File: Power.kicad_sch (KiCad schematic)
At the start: 56 parts, among them IC701 TPS63021DSJR, U702 TLV9304IDR

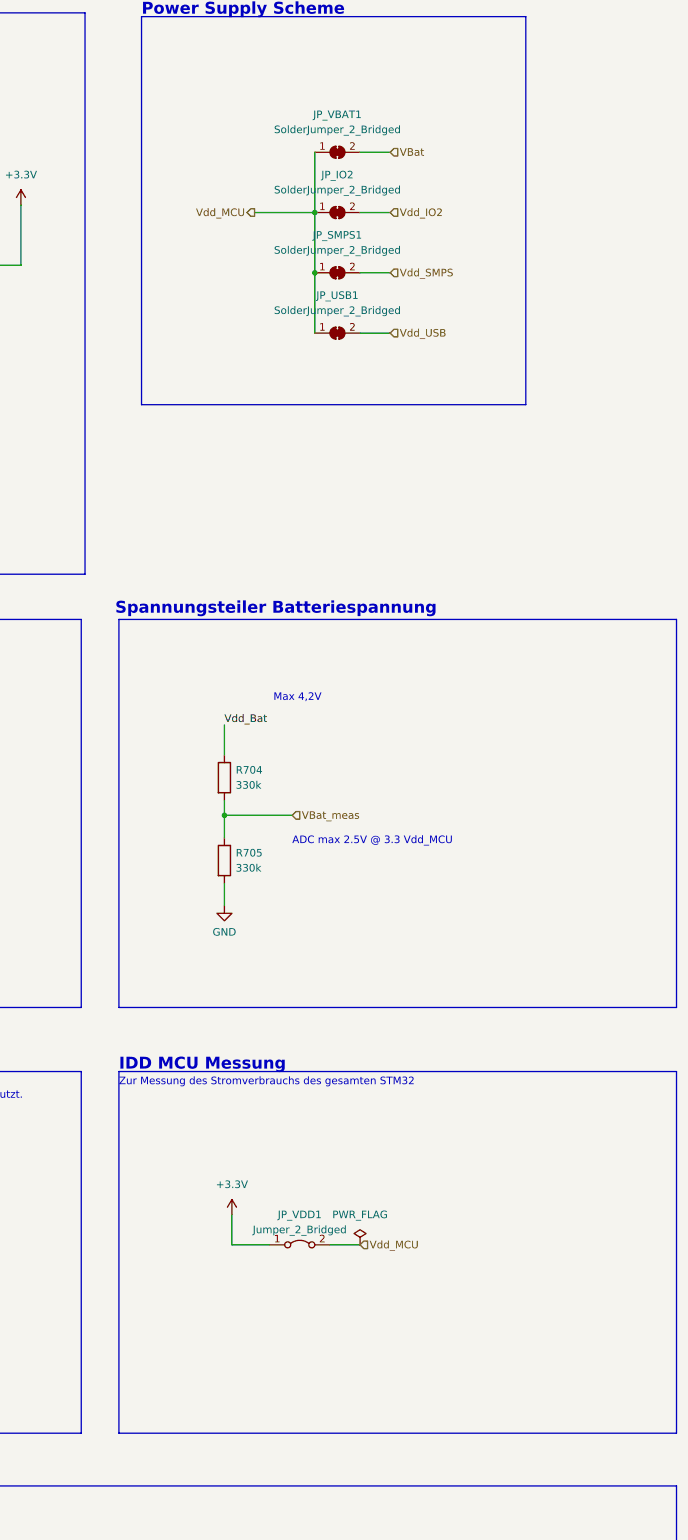
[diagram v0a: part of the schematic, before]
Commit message: Add FC0V104ZFTBR24 component library files
Added symbol, footprint, 3D model, and documentation files for the Supercap (FC0V104ZFTBR24) component across multiple EDA tool formats. Also updated schematic files and project backups, and removed obsolete autosave and backup files.
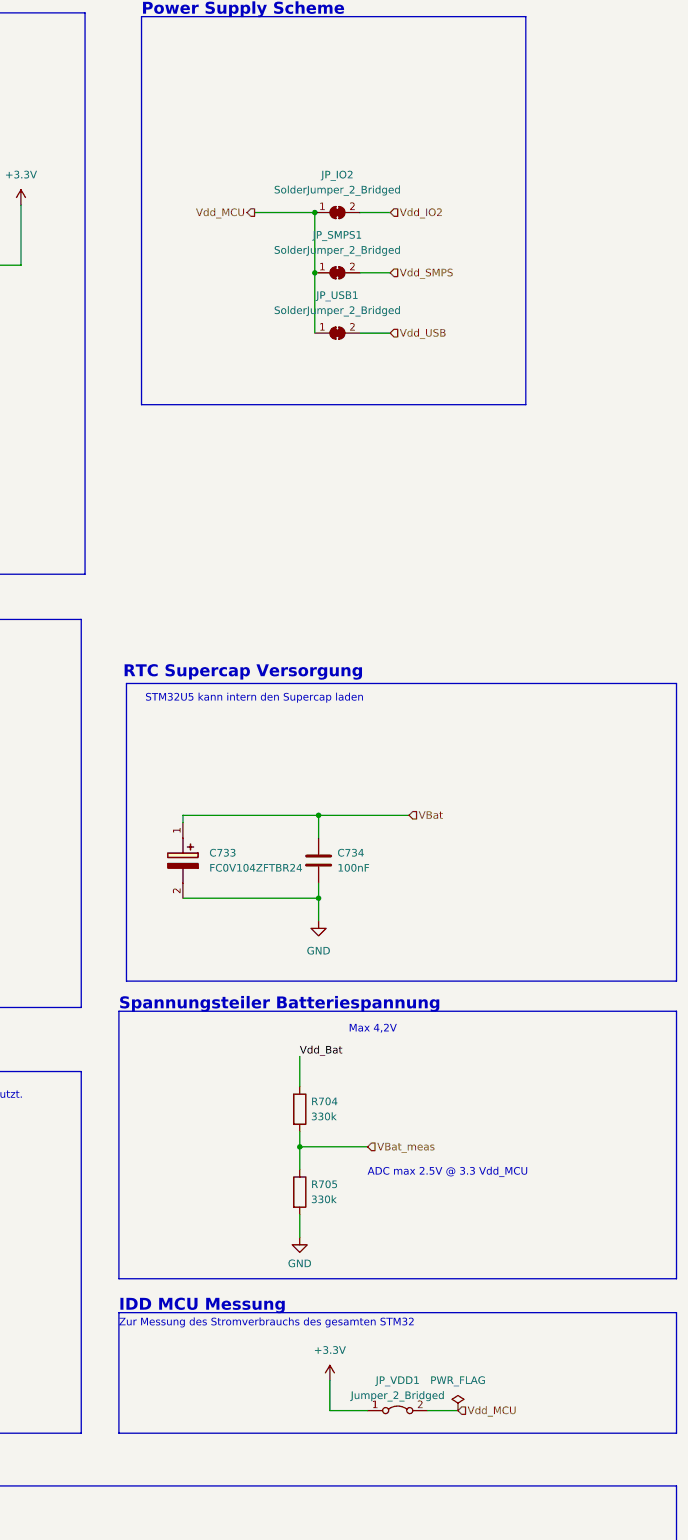
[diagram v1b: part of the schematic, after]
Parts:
- removed JP_VBAT1: SolderJumper_2_Bridged, Jumper:SolderJumper-2_P1.3mm_Open_RoundedPad1.0x1.5mm, symbol Jumper:SolderJumper_2_Bridged
- added C733: FC0V104ZFTBR24, CAPAE1080X550N, symbol SamacSys_Parts:FC0V104ZFTBR24
- added C734: 100nF, symbol Device:C
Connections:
- net GND: now also C733.2 (-), C734.2
- net VBat: now also C733.1 (+), C734.1
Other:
- note added: "RTC Supercap Versorgung"
- note added: "STM32U5 kann intern den Supercap laden"
- moved on the sheet: JP_VDD1, R704, R705

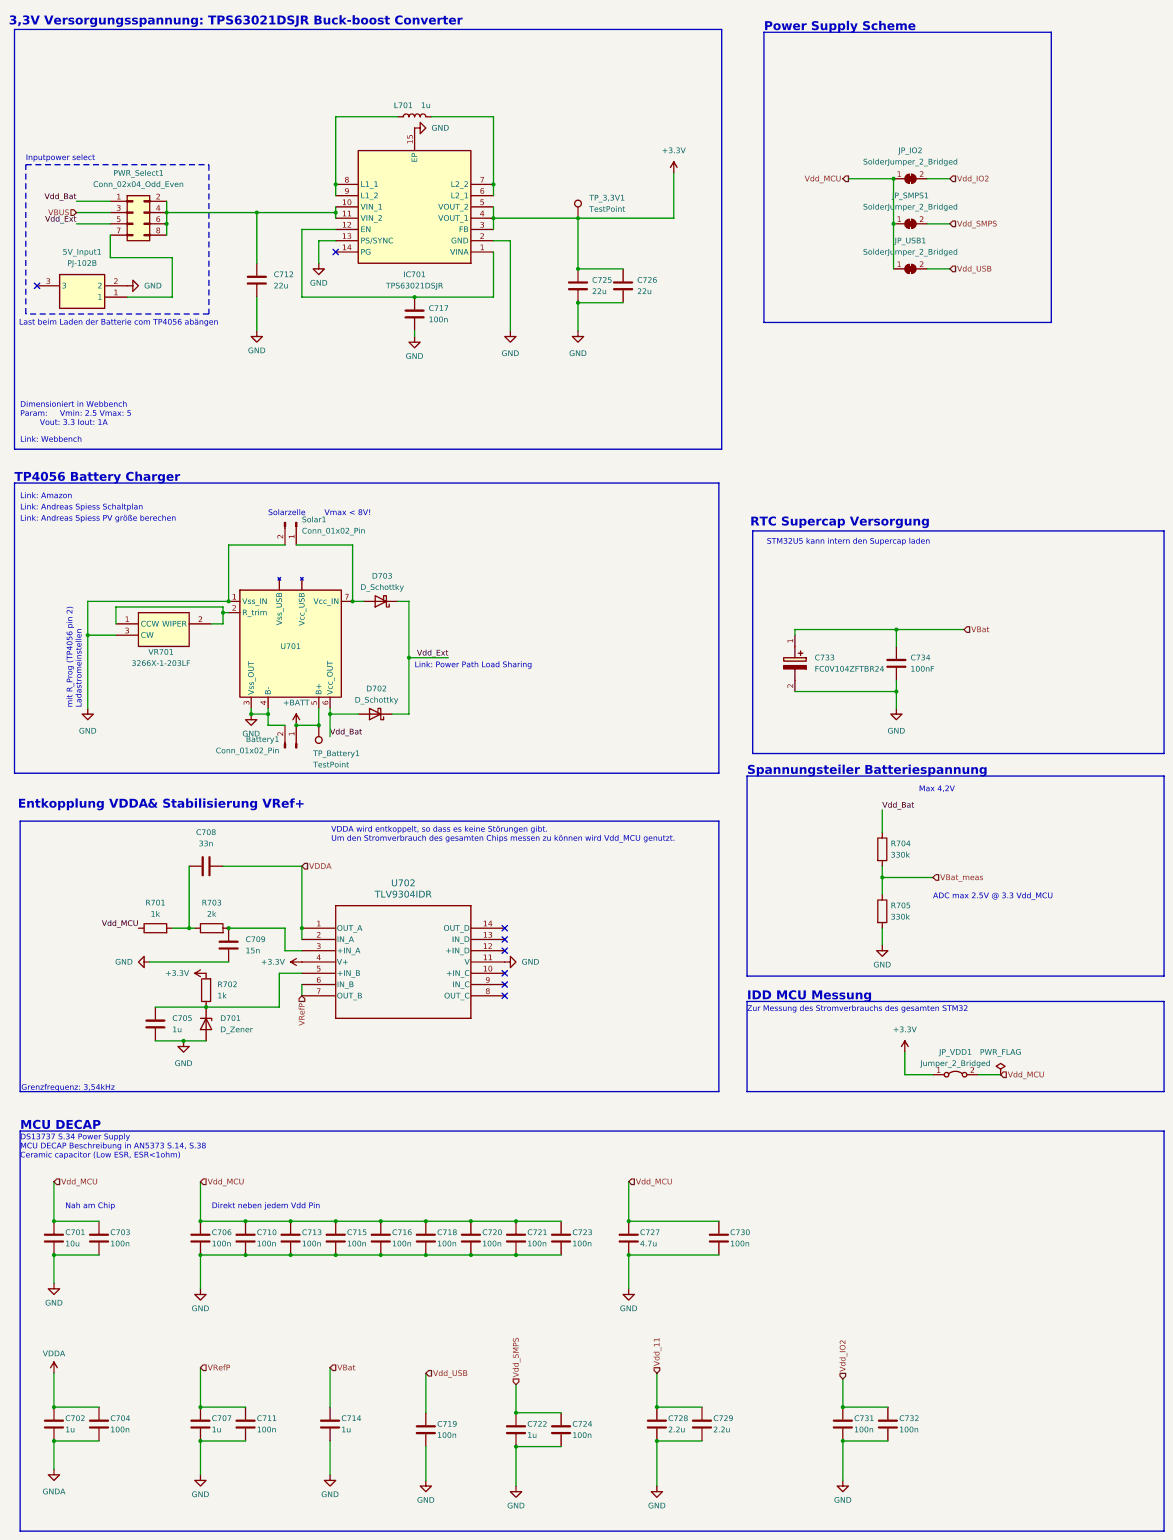
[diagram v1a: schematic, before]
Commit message: Add TP4056-18650 footprint and update Power schematic
Added the TP4056-18650-2 footprint to the library and assigned it to the battery charger in Power.kicad_sch. Updated the Power schematic to improve symbol details, add descriptive properties, and enhance the 3V3 lane toggling section. Made various net and annotation adjustments, and removed obsolete autosave and lock files.
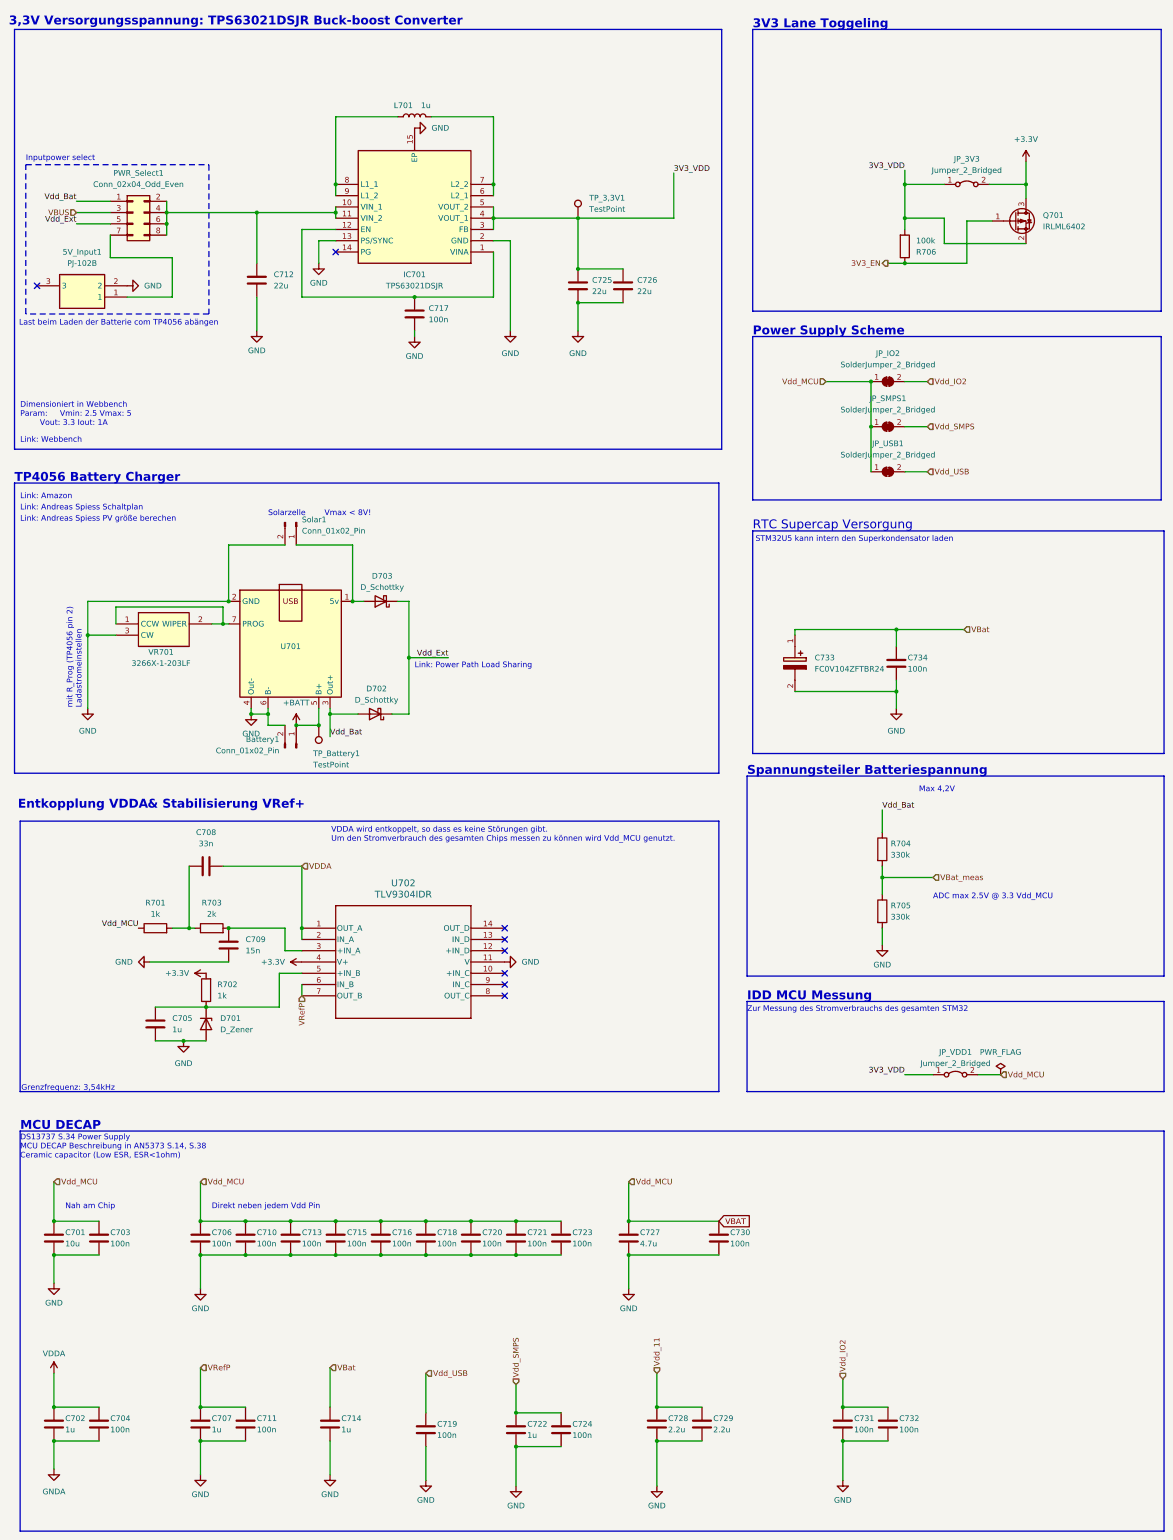
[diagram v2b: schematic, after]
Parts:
- added JP_3V3: Jumper_2_Bridged, Connector_PinHeader_2.54mm:PinHeader_1x02_P2.54mm_Vertical, symbol Jumper:Jumper_2_Bridged
- added Q701: IRLML6402, Package_TO_SOT_SMD:SOT-23, symbol Transistor_FET:IRLML6402
- added R706: 100k, Resistor_SMD:R_0805_2012Metric_Pad1.20x1.40mm_HandSolder, symbol Device:R
- C734: value 100nF -> 100n; footprint (none) -> Capacitor_SMD:C_0805_2012Metric_Pad1.18x1.45mm_HandSolder; Mouser Part Number (none) -> 603-CC805KRX7R9BB104
- U701: footprint TP4056:TP4056-18650 -> TP4056:TP4056-18650-2; DESCRIPTION LiPo Ladeplatine -> Battery Charger 1A
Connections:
- net +3.3V: now also JP_3V3.2 (B), Q701.3 (D); no longer C725.1, C726.1, IC701.3 (FB), IC701.4 (VOUT_1), IC701.5 (VOUT_2), JP_VDD1.1 (A), TP_3,3V1.1
- net GND: now also U701.2 (GND), U701.6 (B-); no longer U701.1 (Vss_IN), U701.3 (Vss_OUT)
- net Vdd_Bat: now also U701.3 (Out+); no longer U701.6 (Vcc_OUT)
- net at D703.2 (A), Solar1.1 (Pin_1): now also U701.1 (5v); no longer U701.7 (Vcc_IN)
- net at VR701.1 (CCW), VR701.2 (WIPER): now also U701.7 (PROG); no longer U701.2 (R_trim)
- net Vdd_MCU renamed VBAT
- new net 3V3_EN: Q701.1 (G), R706.1
- new net 3V3_VDD: C725.1, C726.1, IC701.3 (FB), IC701.4 (VOUT_1), IC701.5 (VOUT_2), JP_3V3.1 (A), JP_VDD1.1 (A), Q701.2 (S), R706.2, TP_3,3V1.1
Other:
- note added: "3V3 Lane Toggeling"
- note added: "STM32U5 kann intern den Superkondensator laden"
- note removed: "STM32U5 kann intern den Supercap laden"
- moved on the sheet: JP_IO2, JP_SMPS1, JP_USB1
